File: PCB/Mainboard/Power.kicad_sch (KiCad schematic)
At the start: 20 parts, among them Q1 P-Channel, U4 AP63357DV-7, U5 TPS2111

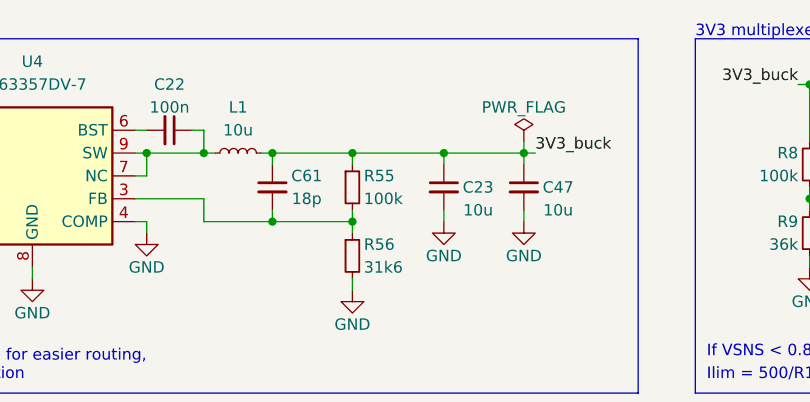
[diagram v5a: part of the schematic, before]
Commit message: Mainboard: version 1.1.2
Add testpoints for power rail testing
Move backside info and logo from mask to silkscreen
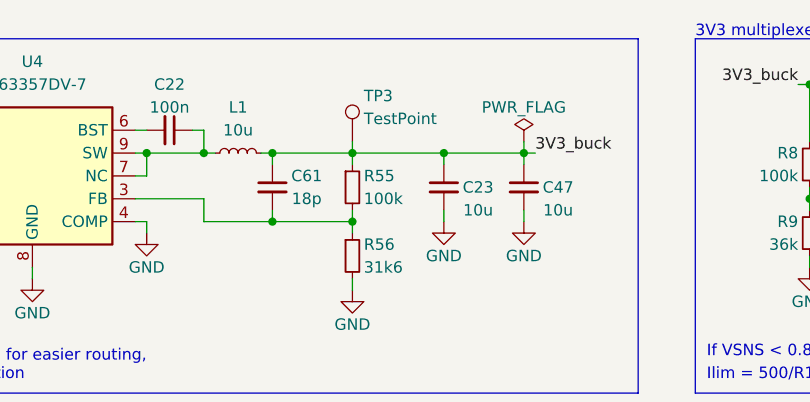
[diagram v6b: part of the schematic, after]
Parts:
- added TP3: TestPoint, TestPoint:TestPoint_Pad_D1.0mm, symbol Connector:TestPoint
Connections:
- net 3V3_buck: now also TP3.1
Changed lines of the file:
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@@
   (title_block
     (title "4x38W amp with DSP and BT")
-    (date "2022-04-17")
-    (rev "1.1.1")
+    (date "2022-04-29")
+    (rev "1.1.2")
     (company "ZOUDIO")
   )
@@
   )
   (wire (pts (xy 135.89 92.71) (xy 135.89 91.44))
+    (stroke (width 0) (type default) (color 0 0 0 0))
+  )
+  (wire (pts (xy 125.73 83.82) (xy 125.73 85.09))
     (stroke (width 0) (type default) (color 0 0 0 0))
   )
@@
     (pin "9")
   )
+  (symbol (lib_id "Connector:TestPoint") (at 125.73 83.82 0) (unit 1)
+    (in_bom yes) (on_board yes)
+    (property "Reference" "TP3" (id 0) (at 127 78.74 0)
+      (effects (font (size 1.27 1.27)) (justify left))
+    )
+    (property "Value" "TestPoint" (id 1) (at 127 81.28 0)
+      (effects (font (size 1.27 1.27)) (justify left))
+    )
+    (property "Footprint" "TestPoint:TestPoint_Pad_D1.0mm" (id 2) (at 130.81 83.82 0)
+      (effects (font (size 1.27 1.27)) hide)
+    )
+    (property "Datasheet" "~" (id 3) (at 130.81 83.82 0)
+      (effects (font (size 1.27 1.27)) hide)
+    )
+    (property "Config" "dnp" (id 4) (at 125.73 83.82 90)
+      (effects (font (size 1.27 1.27)) hide)
+    )
+    (pin "1")
+  )
   (symbol (lib_id "power:GND") (at 125.73 100.33 0) (unit 1)
